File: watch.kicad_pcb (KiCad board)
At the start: 2 copper layers, 35 x 34 mm, 81 parts, among them CON1 USB-MICRO-B, P1 CONN_6, SW1 SW_PUSH, SW2 SW_PUSH, SW3 SW_PUSH, SW4 SW_PUSH, U1 nrf51822, U2 ER-OLED015-1, U3 S25FL1-K, U4 74AHC1G14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

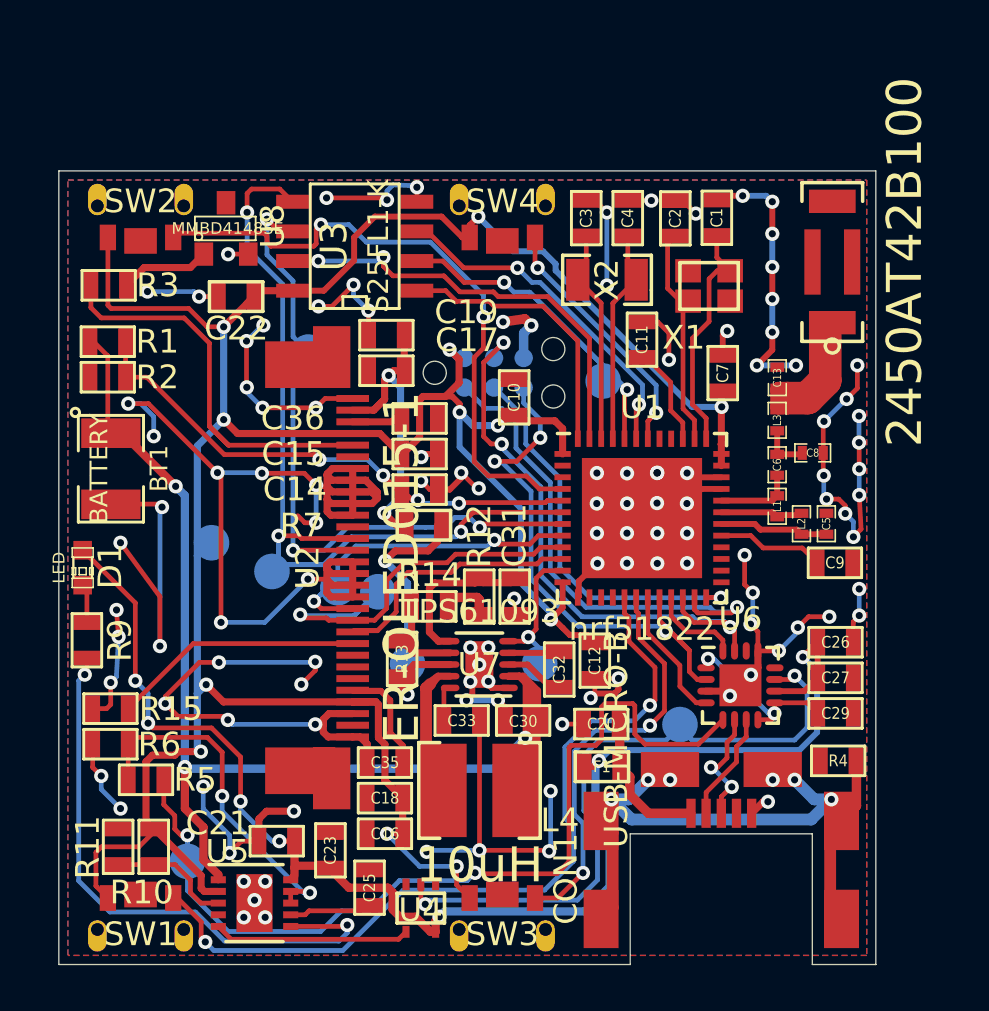
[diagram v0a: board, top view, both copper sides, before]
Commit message: Added missing 2.2uF cap to LTC4063 LDO output, normalized capacitor values to micro and pico, removed units from component values
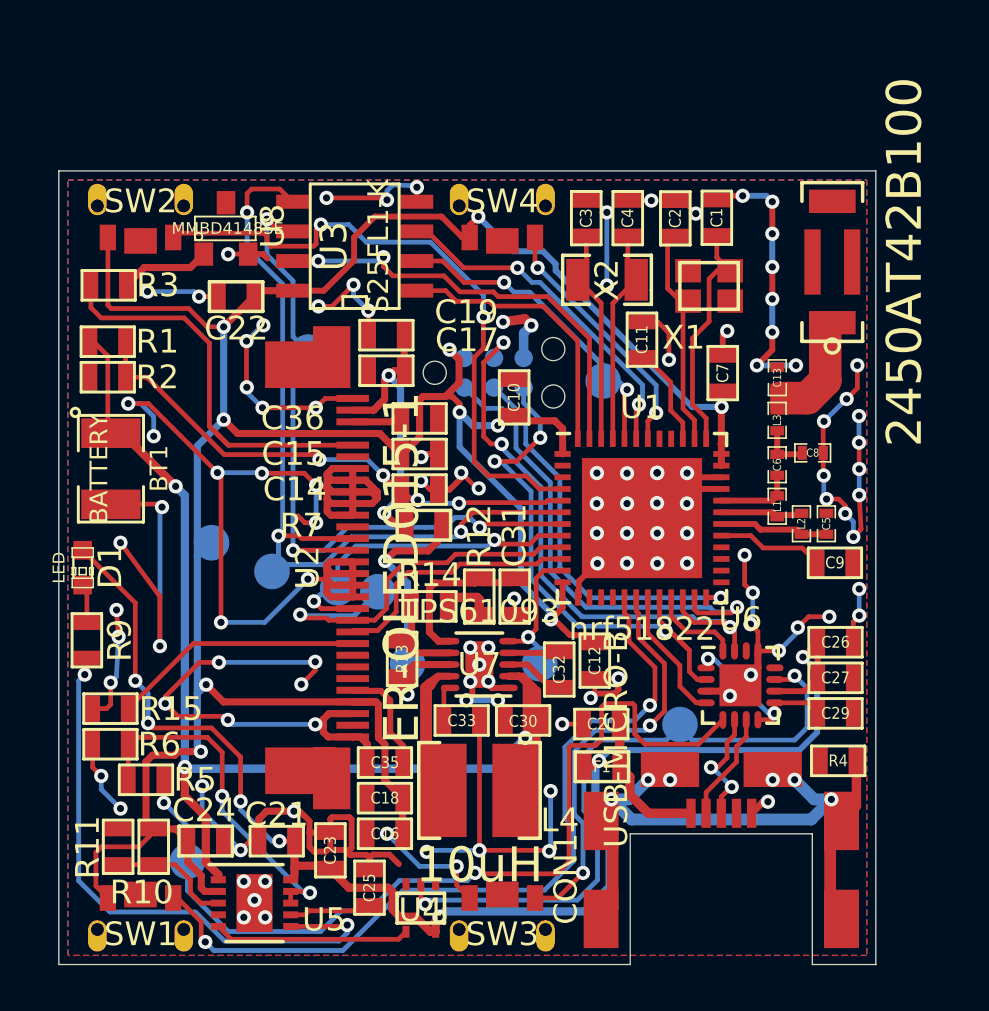
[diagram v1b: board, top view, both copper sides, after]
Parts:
- added C24: 2.2u, SMD_Packages:SMD-0603, F.Cu at (66.3, 88.7)
- C1, C2, C3, C4: value 12pF -> 12p
- C10, C11, C12, C22, C23, C25, C26, C29, C32, C33: value 100nF -> 0.1u
- C13: value 1.5pF -> 1.5p
- C14: value 22nF -> 0.022u
- C18, C19: value 100n -> 0.1u
- C20: value 10nF -> 0.01u
- C21, C31: value 1uF -> 1u
- C27: value 4.7uF -> 0.1u
- C30: value 4.7uF -> 4.7u
- C5: value 2.2nF -> 2200p
- C6: value 2.2pF -> 2.2p
- C7: value 1nF -> 1000p
- C8: value 1pF -> 1p
- C9: value 47nF -> 0.047u
- L1: value 4.7nH -> 4.7n
- L2: value 10nH -> 10n
- L3: value 3.3nH -> 3.3n
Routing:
- net GND: track 239.5 -> 250.9 mm
- net /watch_usb_power/~PWREN: track 40.0 -> 41.0 mm
- net +3.3V: track 134.1 -> 134.7 mm

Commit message: Fixed footprints for MCU and USB-UART, added testpoints
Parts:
- removed BT1: BATTERY, SMD_Packages:SMD-1210
- added -BAT+: BATTERY, SMD_Packages:SMD-1210, F.Cu at (62.2, 72.8)
- added TP1: TST, Measurement_Points:Measurement_Point_Round-SMD-Pad_Small, B.Cu at (89.4, 77.2)
- added TP12: TST, Measurement_Points:Measurement_Point_Round-SMD-Pad_Small, B.Cu at (91.4, 77.2)
- added TP15: TST, Measurement_Points:Measurement_Point_Round-SMD-Pad_Small, B.Cu at (93.4, 77.2)
- C24: value 2.2u -> 2200p
- U1: footprint Housings_DFN_QFN:QFN-48-1EP_7x7mm_Pitch0.5mm -> Housings_QFN_DFN:UQFN-48-1EP_6x6mm_Pitch0.4mm
- U6: footprint Housings_DFN_QFN:QFN-16-1EP_3x3mm_Pitch0.5mm -> Housings_QFN_DFN:QFN-16-1EP_4x4mm_Pitch0.65mm
- moved U6 1.06 mm to (88.4, 81.3)
- moved U1 0.81 mm to (85.6, 74.3)
- moved C26 0.71 mm to (93.3, 79.5)
- moved C27 0.71 mm to (93.3, 81.0)
- moved C13 0.60 mm to (90.4, 68.4)
- moved C5 0.60 mm to (92.5, 74.6)
- moved C6 0.60 mm to (90.4, 72.1)
- moved L2 0.60 mm to (91.5, 74.6)
- moved L3 0.60 mm to (90.4, 70.2)
- moved C8 0.60 mm to (91.9, 71.6)
- moved L1 0.60 mm to (90.4, 73.9)
- moved C9 0.45 mm to (93.2, 76.3)
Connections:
- ANT1 pad 2: (no net) -> Net-(ANT1-Pad2)
- ANT1 pad 3: (no net) -> Net-(ANT1-Pad3)
- ANT1 pad 4: (no net) -> Net-(ANT1-Pad4)
- CON1 pad 4: (no net) -> Net-(CON1-Pad4)
- U1 pad 14: (no net) -> Net-(U1-Pad14)
- U1 pad 15: (no net) -> /SW1
- U1 pad 16: (no net) -> /SW3
- U1 pad 17: /SW1 -> Net-(U1-Pad17)
- U1 pad 18: /SW3 -> MCU_RTS
- U1 pad 19: MCU_RTS -> MCU_TX
- U1 pad 2: (no net) -> Net-(U1-Pad2)
- U1 pad 20: MCU_TX -> MCU_CTS
- U1 pad 21: MCU_CTS -> MCU_RX
- U1 pad 22: MCU_RX -> Net-(U1-Pad22)
- U1 pad 25: (no net) -> Net-(U1-Pad25)
- U1 pad 26: (no net) -> Net-(U1-Pad26)
- U1 pad 27: (no net) -> Net-(U1-Pad27)
- U1 pad 28: (no net) -> Net-(U1-Pad28)
- U1 pad 3: (no net) -> Net-(U1-Pad3)
- U1 pad 40: (no net) -> Net-(U1-Pad40)
- U1 pad 41: (no net) -> Net-(U1-Pad41)
- U2 pad 12: (no net) -> Net-(U2-Pad12)
- U2 pad 23: (no net) -> Net-(U2-Pad23)
- U2 pad 24: (no net) -> Net-(U2-Pad24)
- U2 pad 25: (no net) -> Net-(U2-Pad25)
- U2 pad 29: (no net) -> Net-(U2-Pad29)
- U2 pad 6: (no net) -> Net-(U2-Pad6)
- U5 pad 4: (no net) -> Net-(U5-Pad4)
- U6 pad 12: (no net) -> Net-(U6-Pad12)
- U6 pad 14: (no net) -> Net-(U6-Pad14)
- U8 pad 3: (no net) -> Net-(U8-Pad3)
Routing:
- net GND: track 250.9 -> 224.7 mm, vias 118 -> 107
- net /watch_usb_power/~SLEEP: track 28.4 -> 32.4 mm
- net /MISO: track 19.7 -> 16.1 mm
- net DISP_EN: track 6.44 -> 9.67 mm
- net +3.3V: track 134.7 -> 137.6 mm
- net Net-(C29-Pad1): track 8.86 -> 11.5 mm
- net MCU_TX: track 23.3 -> 20.9 mm
- net MCU_RX: track 25.5 -> 23.1 mm
- net /WP_MEM: track 15.7 -> 17.3 mm
- net /SWDIO: track 21.1 -> 22.6 mm
- net CS_DISP: track 12.0 -> 13.4 mm
- net DC_DISP: track 18.6 -> 19.9 mm
- net Net-(C14-Pad2): track 22.5 -> 23.8 mm
- net RST_DISP: track 15.2 -> 16.5 mm
- net SCK: track 32.7 -> 33.9 mm
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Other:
- board size 35 x 34 mm -> 35 x 34.5 mm
- board text added: "BLE HRM WATCH V1.1"
- board text removed: "BLE HRM WATCH V1.0"
